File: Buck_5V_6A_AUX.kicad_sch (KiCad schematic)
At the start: 10 parts, among them U5 PTPSM63606RDLR

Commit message: Rename power nets, add mounting holes, retitle sheet 1, clear ERC
Power nets, no commas, named by function:
- "+5V, 2A" -> +5V_SYS, "+5V, 6A PI" -> +5V_PI, "+5V, 6A AUX" -> +5V_AUX
Buck sheets renamed to Buck 5V SYS / Buck 5V PI / Buck 5V AUX. Notes,
descriptions, README and docs updated.

Mechanical and title:
- H1-H4: M3 mounting holes, 3.2 mm plated, isolated (no net), not in BOM
- Sheet 1 title: "Delivery Robot Main Board"

ERC, now 0 errors and 0 warnings (was 4 errors, 15 warnings):
- PWR_FLAGs on +12V (after F1), GND (at J2), +3.3VA (after FB2) and
  +5V_SYS (after the TPS54202's L1)
- TPSM63606 symbol pin types set (VOUT power out, FB/EN input, VIN/
  VLDOIN/GND power in, PG open collector, others passive) in both buck
  sheets and libs/TPSM63606RDLR.kicad_sym
- U1 STM32F091RCTx and Y3 Crystal_GND24 moved to a new
  libs/project_symbols.kicad_sym holding the versions this design uses
  (the current KiCad library moved their pins); libs/TPS54202DDCR made
  to match the schematic's U3
Connectivity unchanged: same 108 nets and pins.

Co-Authored-By: Claude Opus 5.5 <noreply@anthropic.com>
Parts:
- U5: Used In Sheet Buck_5V_6A_AUX: 12 V in, +5V, 6A AUX net out -> Sheet Buck_5V_6A_AUX: 12 V in, +5V_AUX net out
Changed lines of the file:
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@@
 			)
 		)
-		(property "Used In" "Sheet Buck_5V_6A_AUX: 12 V in, +5V, 6A AUX net out"
+		(property "Used In" "Sheet Buck_5V_6A_AUX: 12 V in, +5V_AUX net out"
 			(at 115.57 86.36 0)
 			(hide yes)

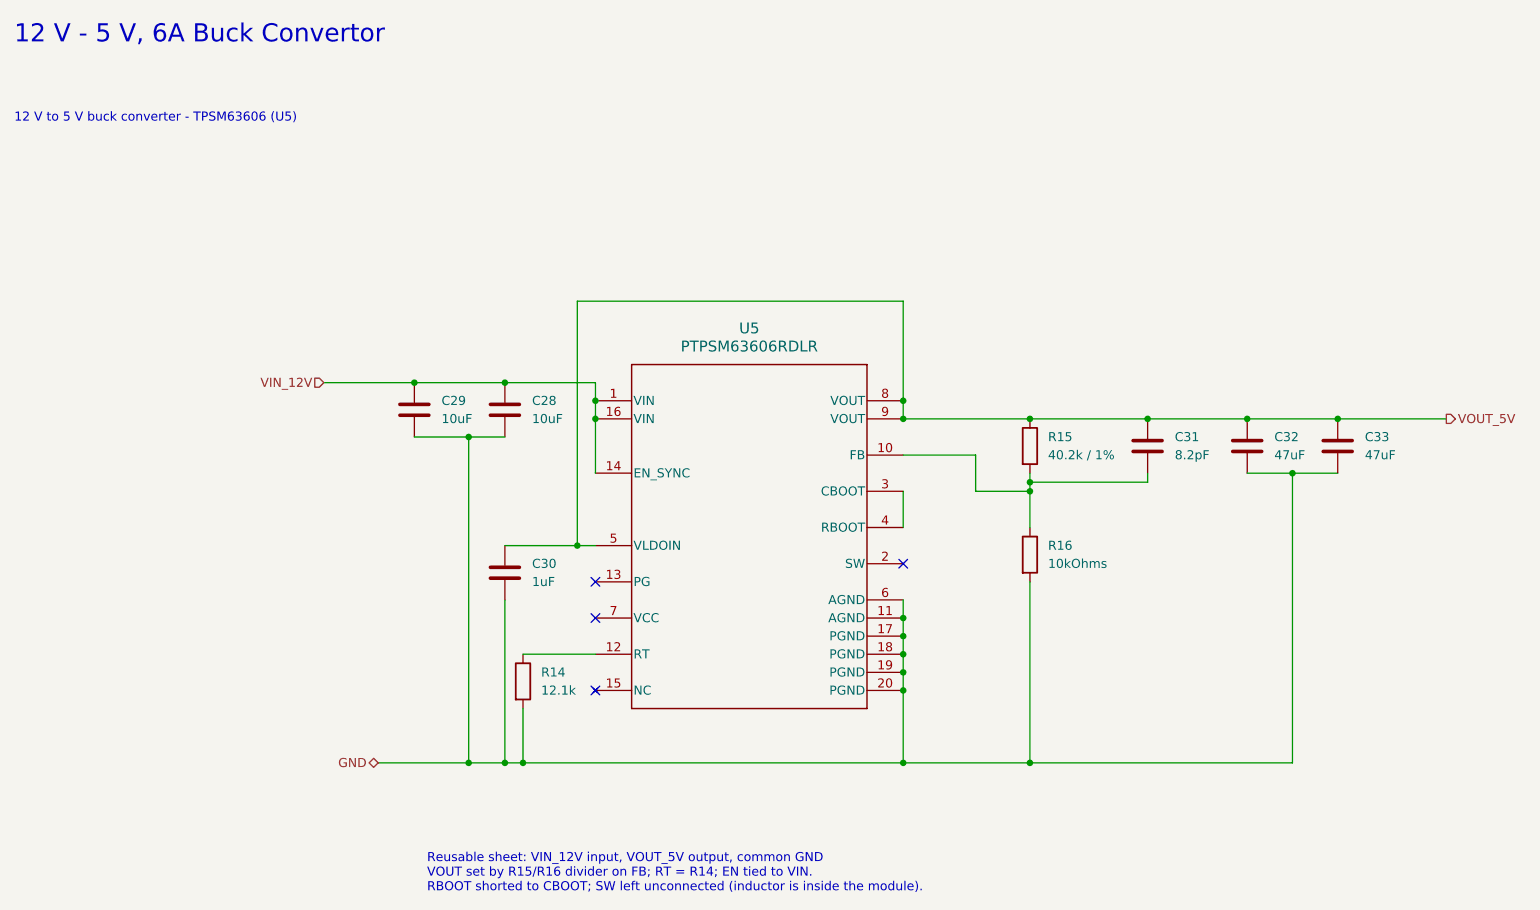
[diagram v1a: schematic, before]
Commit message: Add input protection, AUX ports, servo interface and Pi control
Implements the 2026-10-15 design review decisions in the schematic.
ERC 0 errors, 0 warnings.

New sheets:
- Input Protection: Q1 SQJ409EP reverse-battery P-FET after F1 (D12
  12 V gate clamp, R36), D13 SMBJ16A TVS on +12V, battery sense
  R37/R38/C37 -> VBAT_SENSE on PA0. PWR_FLAG moves to +12V.
- AUX Outputs: four +5V_AUX ports J18-J21 (JST XH 2-pin: Notecard,
  LiDAR, GNSS, IMU), each through a 1.5 A PTC (F4-F7).
- Servo Interface: J17 (GND, VBAT_SERVO via F3 5 A fuse, SERVO_SIG) for
  the Hiwonder HTS-30HS through an external 11.1-12 V buck. U8
  SN74LVC1T45 translates PB10 (USART3 half-duplex) to the 5 V bus,
  PB11 sets direction; R39-R42 pull-ups/series, D14 ESD.

Root sheet:
- F1 output is now VBAT_FUSED; C36 sits on +12V after Q1. J2-F1 net
  named VBAT_IN. F1 7.5 A -> 10 A (0297010.L).
- Y3/C5/C6 fitted (were DNP).
- PA0 -> VBAT_SENSE, PA1 -> PI_3V3_SENSE, PB10 -> SERVO_TX,
  PB11 -> SERVO_DIR. Notes updated (no more F2 / XT30-only text).

Pi 5 Interface:
- J13 -> 6-pin JST XH: TXD, RXD, GND, PI_3V3, PI_RESET, PI_BOOT0.
- PI_3V3 -> D15 -> AUX_EN (U5 enable) and R44/R45 -> PA1.
- PI_RESET -> Q2 DMN63D8L -> NRST (open drain, R46 pull-down).
- PI_BOOT0 -> R47 1k -> BOOT0, for reflashing over USART2.
- R12/R13 100R -> 1k (PA2/PA3 are TTa, 5 mA injection max).
- Remove TP2 (same net as TP1 since F2 was removed).

Buck 5V AUX: U5 EN from AUX_EN (was +12V), R43 100k pull-down, C40,
J22 force-on jumper. Buck 5V SYS: C49 100 nF at U3 VIN/GND.
U2/U5 value TPSM63606RDLR; VCC design note corrected (internal 1 uF,
must stay NC).

Motor Control (now A3):
- U9/U10 74LVC2G17 encoder buffers on +3V3; encoder series R 100R ->
  1k with C43-C46 1 nF; R48-R51 4.7k pull-ups (DNP).
- F8/F9 0.2 A PTC + C47/C48 on each encoder supply (ENC1_5V, ENC2_5V).
- J7/J15 pin order 5V, GND, A, B (matches the am-3651 plug).
- R52/R53 10k pull-downs on both PWM lines (MDD20A brakes on low).
- F10/F11 PTC in series with J6/J16 p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
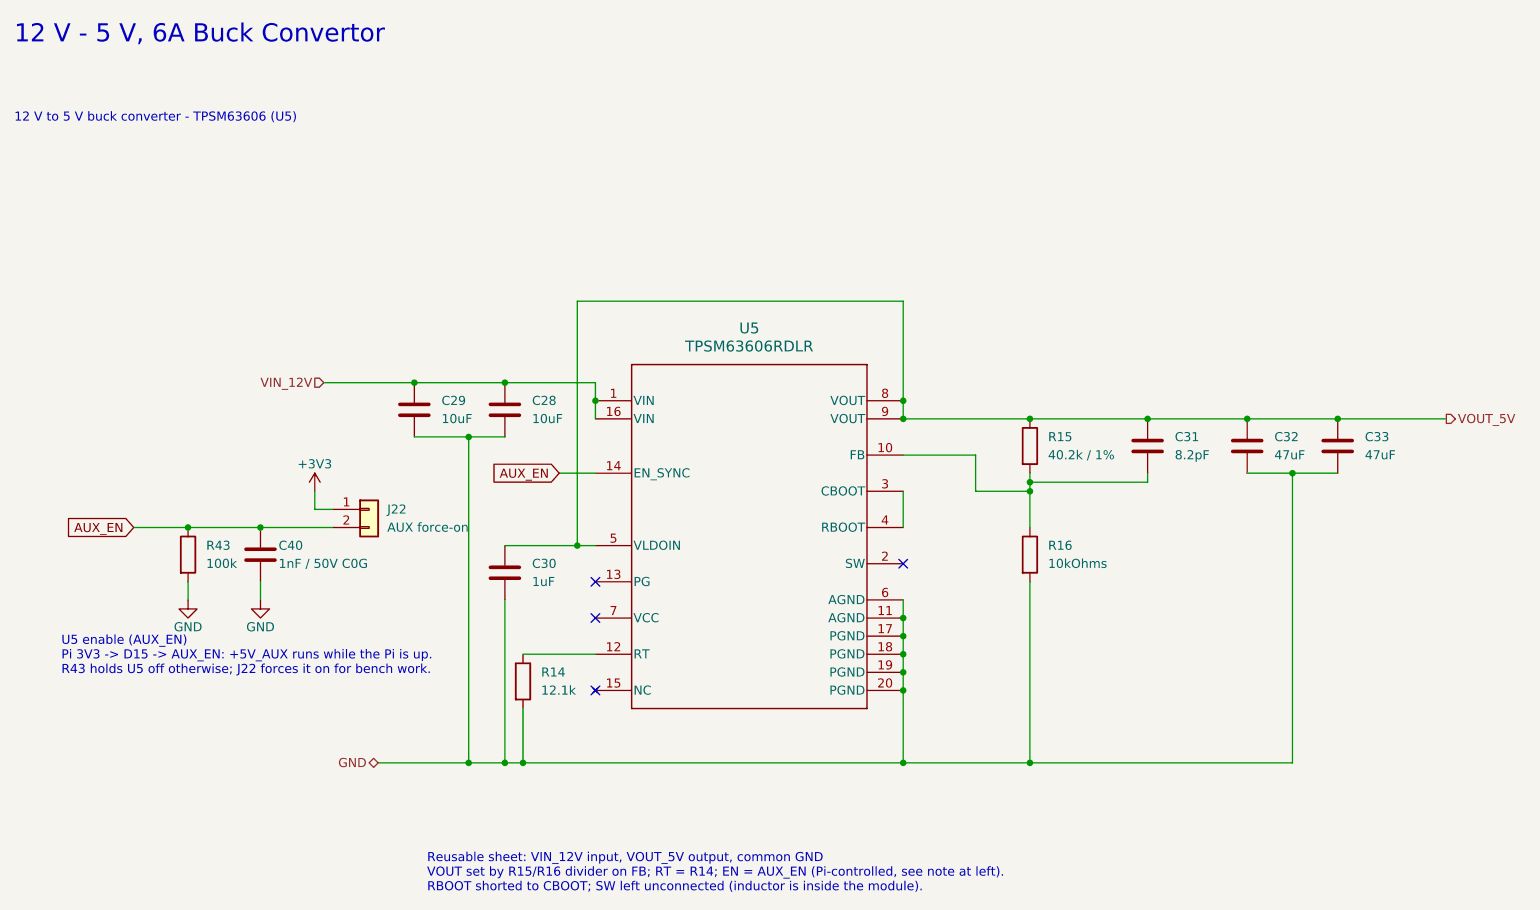
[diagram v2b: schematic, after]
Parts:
- added C40: 1nF / 50V C0G, Capacitor_SMD:C_0603_1608Metric, symbol Device:C
- added J22: AUX force-on, Connector_PinHeader_2.54mm:PinHeader_1x02_P2.54mm_Vertical, symbol Connector_Generic:Conn_01x02
- added R43: 100k, Resistor_SMD:R_0805_2012Metric, symbol Device:R
- U5: value PTPSM63606RDLR -> TPSM63606RDLR; Design Notes VOUT = VREF x (1 + R15/R16) with FB divider R15 40.2k / R16 10k (VOUT = 5.02 V), C31 feed-forward; RT = R14 12.1k; EN tied to VIN; RBOOT shorted to CBOOT; SW pin left NC; PG open-drain, unused; VLDOIN tied to VOUT; VCC needs 1 uF to AGND per datasheet - CHECK C30 placement (currently on VLDOIN/VOUT, VCC flagged NC) -> VOUT = VREF x (1 + R15/R16) with FB divider R15 40.2k / R16 10k (VOUT = 5.02 V), C31 feed-forward; RT = R14 12.1k; EN = AUX_EN (Pi 3V3 through D15, 100k pull-down R43, force-on jumper J22); RBOOT shorted to CBOOT; SW pin left NC; PG open-drain, unused; VLDOIN tied to VOUT; VCC has an internal 1 uF and must not be loaded (SLVSGB4B pin table), so it is left NC; C30 is the VLDOIN capacitor; MPN TPSM63606RDLR (schematic symbol: PTPSM63606RDLR) -> TPSM63606RDLR
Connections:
- net GND: now also C40.2, R43.2
- net VIN_12V: no longer U5.14 (EN_SYNC)
- new net +3V3: J22.1 (Pin_1)
- new net AUX_EN: C40.1, J22.2 (Pin_2), R43.1, U5.14 (EN_SYNC)
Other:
- note added: "Reusable sheet: VIN_12V input, VOUT_5V output, common GND VOUT set by R15/R16 divider on FB; RT = R14; EN = AUX_EN (Pi-controlled, see note at left). RBOOT shorted to CBOOT; SW left unconnected (inductor is inside the module)."
- note added: "U5 enable (AUX_EN) Pi 3V3 -> D15 -> AUX_EN: +5V_AUX runs while the Pi is up. R43 holds U5 off otherwise; J22 forces it on for bench work."
- note removed: "Reusable sheet: VIN_12V input, VOUT_5V output, common GND VOUT set by R15/R16 divider on FB; RT = R14; EN tied to VIN. RBOOT shorted to CBOOT; SW left unconnected (inductor is inside the module)."
